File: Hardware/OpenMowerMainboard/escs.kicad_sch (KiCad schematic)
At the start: 46 parts, among them J15 Conn_02x02_Female, J24 Conn_01x06_Female, J25 Conn_02x02_Female, J26 Conn_01x06_Female, J27 Conn_02x02_Female, J28 Conn_01x05_Female, J29 Conn_01x05_Female, J30 Conn_01x09_Female, J31 Conn_02x02_Female, J32 Conn_01x06_Female, J33 Conn_02x02_Female, J34 Conn_01x06_Female, J35 Conn_02x02_Female, J36 Conn_01x05_Female, J37 Conn_01x05_Female, J38 Conn_01x09_Female, J39 Conn_02x02_Female, J40 Conn_01x06_Female, J41 Conn_02x02_Female, J42 Conn_01x06_Female, J43 Conn_02x02_Female, J44 Conn_01x05_Female, J45 Conn_01x05_Female, J46 Conn_01x09_Female, U4 xESC2, U5 xESC2, U6 xESC2

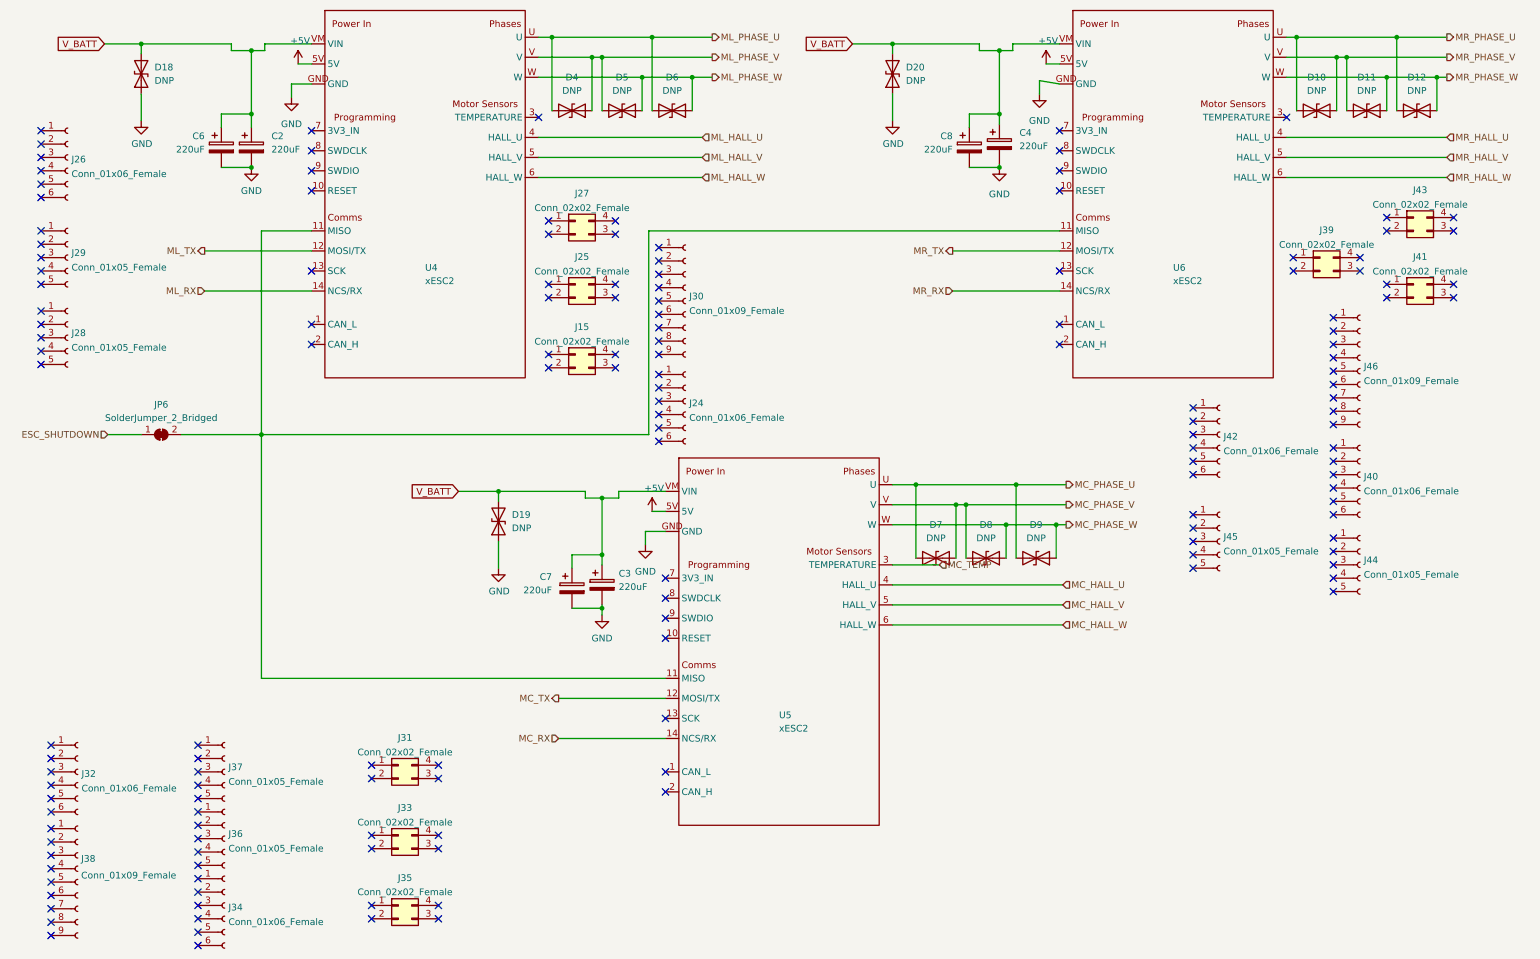
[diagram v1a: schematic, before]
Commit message: feat: update to Kicad7, put back C2,C3
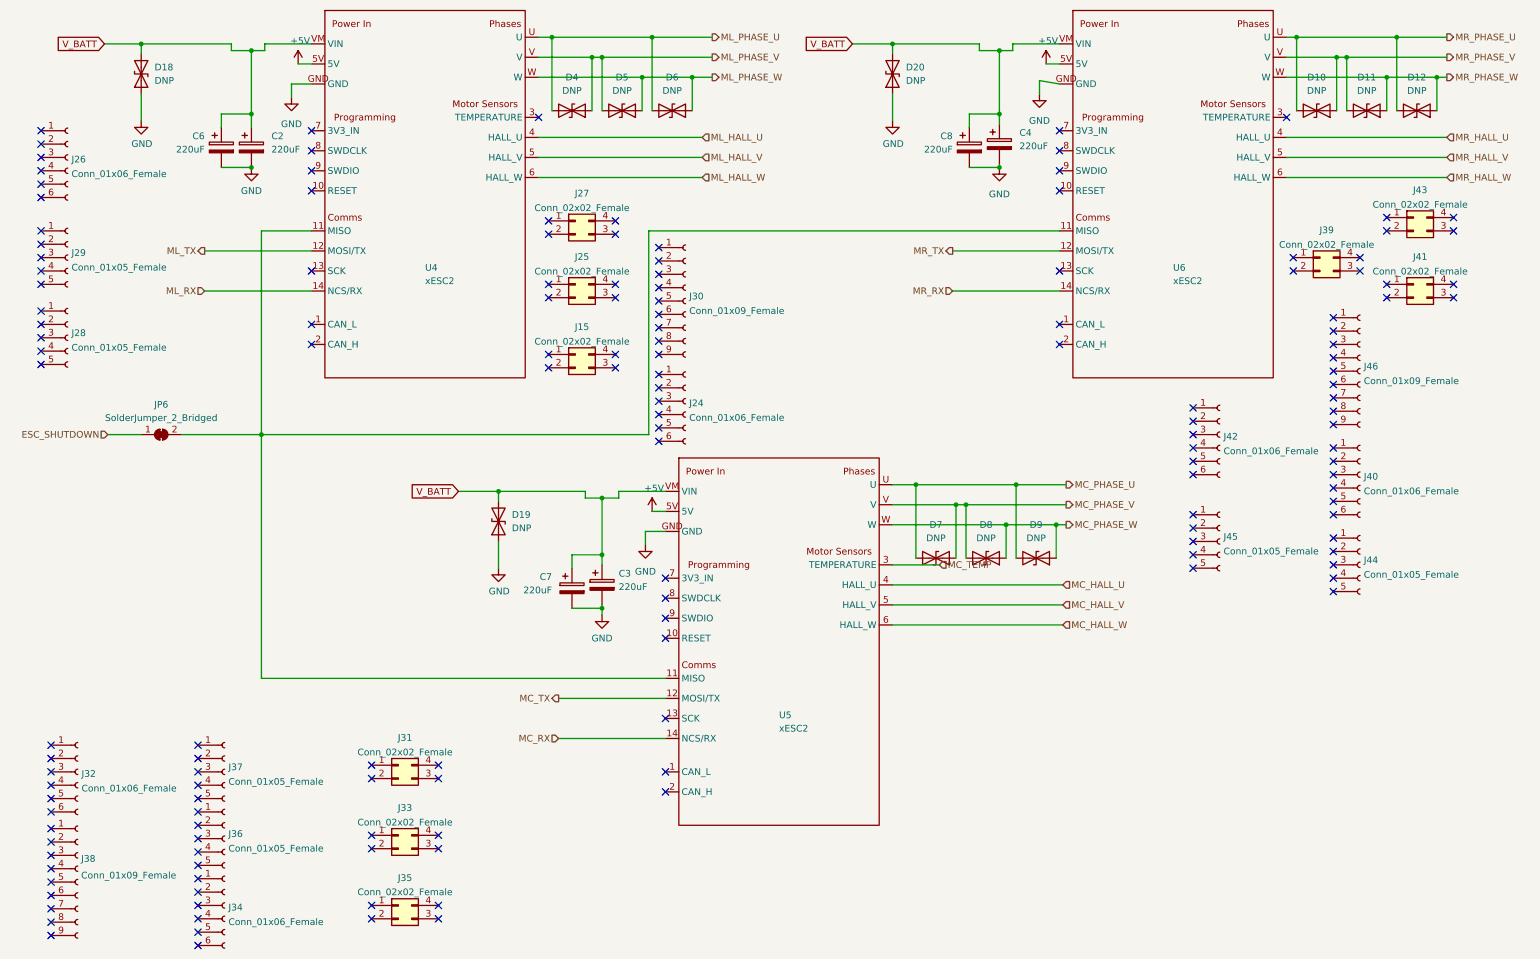
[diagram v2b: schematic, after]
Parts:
- C3, C6: now in the parts list
